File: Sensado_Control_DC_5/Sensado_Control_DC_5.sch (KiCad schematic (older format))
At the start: 30 parts

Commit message: Control DC, y Micro placa 5
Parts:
- removed Q? (x3): NMOS, TO_SOT_Packages_THT:TO-220_Vertical, symbol NMOS
- removed Q? (x3): PMOS, TO_SOT_Packages_THT:TO-220_Vertical, symbol PMOS
- removed R? (x15): R, symbol R
- added C1, C2, C3, C5, C6: 0,1uF, Capacitors_SMD:C_0805_HandSoldering, symbol 0,1uF
- added C4: 1nF, Capacitors_SMD:C_1206_HandSoldering, symbol 1nF
- added C7, C8: 18pF, Capacitors_SMD:C_0805_HandSoldering, symbol 18pF
- added C9: 10uF, Capacitors_SMD:C_0805_HandSoldering, symbol 10uF
- added D1, D2, D3: Led_Small_Reg, LEDs:LED_0805, symbol Led_Small_Reg
- added J1, J2, J3: Jumper, Pin_Headers:Pin_Header_Straight_1x02_Pitch2.54mm, symbol Jumper
- added P10: GPIO, Socket_Strips:Socket_Strip_Straight_1x05_Pitch2.54mm, symbol CONN_01X05
- added P11: CONM_R1, Socket_Strips:Socket_Strip_Straight_1x02_Pitch2.54mm, symbol CONN_01X02
- added P2: I_+, Sockets_MOLEX_KK-System:Socket_MOLEX-KK-RM3-96mm_Lock_2pin_straight, symbol CONN_01X02
- added P3: I_-, Sockets_MOLEX_KK-System:Socket_MOLEX-KK-RM3-96mm_Lock_2pin_straight, symbol CONN_01X02
- added P4: POWER, Sockets_MOLEX_KK-System:Socket_MOLEX-KK-RM3-96mm_Lock_2pin_straight, symbol CONN_01X02
- added P5: RS-232, Socket_Strips:Socket_Strip_Straight_1x03_Pitch2.54mm, symbol CONN_01X03
- added P6: I2C, Socket_Strips:Socket_Strip_Straight_1x02_Pitch2.54mm, symbol CONN_01X02
- added P7: SPI, Socket_Strips:Socket_Strip_Straight_1x04_Pitch2.54mm, symbol CONN_01X04
- added P8: GND_REG, Socket_Strips:Socket_Strip_Straight_1x01_Pitch2.54mm, symbol CONN_01X01
- added P9: RESET, Socket_Strips:Socket_Strip_Straight_1x01_Pitch2.54mm, symbol CONN_01X01
- added Q10, Q14, Q15, Q16, Q7, Q8, Q9: PMOS, TO_SOT_Packages_THT:TO-220_Vertical, symbol PMOS
- added Q11, Q12, Q13, Q2, Q3, Q4, Q5: NMOS, TO_SOT_Packages_THT:TO-220_Vertical, symbol NMOS
- added R10, R11, R13, R14, R15, R16, R18, R19, R2, R20, R21, R23, R24, R25, R26, R27, R28, R29, R3, R30, R31, R32, R33, R34, R35, R36, R37, R38, R39, R4, R40, R41, R5, R8, R9: R, Resistors_THT:R_Axial_DIN0207_L6.3mm_D2.5mm_P7.62mm_Horizontal, symbol R
- added R42, R44, R47: 10K, Resistors_SMD:R_0805_HandSoldering, symbol 10K
- added R43, R45, R46: 1K, Resistors_SMD:R_0805_HandSoldering, symbol 1K
- added U1: Atmega328PA, Housings_QFP:LQFP-32_7x7mm_Pitch0.8mm, symbol Atmega328PA
- added U2: ACS_712, Housings_SOIC:SOIC-8_3.9x4.9mm_Pitch1.27mm, symbol ACS_712
- added U3: LD1117S50TR_FINAL, TO_SOT_Packages_SMD:SOT-223, symbol LD1117S50TR_FINAL
- added Y1: AMB3_16M, symbol AMB3_16M
- P1: renamed from P?; value CONN_01X02 -> R_FUENTE_CON; footprint (none) -> Sockets_MOLEX_KK-System:Socket_MOLEX-KK-RM3-96mm_Lock_2pin_straight
- R1, R12, R17, R22, R7: renamed from R?; footprint (none) -> Resistors_THT:R_Axial_DIN0207_L6.3mm_D2.5mm_P7.62mm_Horizontal
- R6: renamed from R?; footprint (none) -> Resistors_THT:R_Axial_DIN0207_L6.3mm_D2.5mm_P10.16mm_Horizontal
- gave numbers to parts that had none: 2
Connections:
- net labels added: 5V, CLK1, CLK2, I_SENS+, I_SENS-, MISO, MOSI, REG1_1, REG1_2, REG1_3, REG1_4, REG1_5, RESET, RXD, SCK, SCL, SCL_E, SDA, SDA_E, TXD, VCONTROL_2, VCONTROL_3, VCONTROL_4, VCONTROL_5, VCONTROL_6, VCONTROL_7, VCONTROL_8, VOUT_SENS, V_FUENTE, ~SS
- wire segments 62 -> 244
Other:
- note added: "Conector Progrmador \ndel Microcontrolador \n- Debuger (RS-232)"
- note added: "Conectores Fuente Conmutada"
- note added: "GPIO"
- note added: "In Sensor de Corriente"
- note added: "Out Sensor de Corriente"
- note added: "Pines de Alimentacion"
- note added: "Quemador Bootloader -\nComunicacion SPI"
- note added: "Regulador\n"
- note added: "Reset Micro"
- note added: "Resistencias Pull-up\n- Comunicacion I2C"
- note added: "Resistor Variable 1"
- note added: "Resistor Variable 2\n"
- note added: "Resistor Variable 3\n"
- note added: "Resistor Variable 4\n"
- note added: "Resistor Variable 5"
- note added: "Resistor Variable 6"
- note added: "Resistor Variable 7"
- note added: "Resistor Variable 8"
- note added: "Sensor de Corriente\n"
- note added: "Señal de Reloj Externo \n Atmega"
- note added: "Tierra para Alimentacion \nExterna al Regulador"

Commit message: Version avanzada PCB
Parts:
- removed C4: 1nF, Capacitors_SMD:C_1206_HandSoldering, symbol 1nF
- removed P11: CONM_R1, Socket_Strips:Socket_Strip_Straight_1x02_Pitch2.54mm, symbol CONN_01X02
- added C4: 1nF_THT, Capacitors_THT:C_Disc_D5.0mm_W2.5mm_P2.50mm, symbol 1nF_THT
- R6: footprint Resistors_THT:R_Axial_DIN0207_L6.3mm_D2.5mm_P10.16mm_Horizontal -> Resistors_THT:R_Axial_DIN0207_L6.3mm_D2.5mm_P7.62mm_Horizontal
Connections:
- wire segments 244 -> 242
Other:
- note removed: "Conectores Fuente Conmutada"
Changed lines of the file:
@@
 F 0 "R6" V 1210 1030 50  0000 C CNN
 F 1 "R" V 1130 1030 50  0000 C CNN
-F 2 "Resistors_THT:R_Axial_DIN0207_L6.3mm_D2.5mm_P10.16mm_Horizontal" V 1060 1030 50  0001 C CNN
+F 2 "Resistors_THT:R_Axial_DIN0207_L6.3mm_D2.5mm_P7.62mm_Horizontal" V 1060 1030 50  0001 C CNN
 F 3 "" H 1130 1030 50  0000 C CNN
 	1    1130 1030
@@
 VOUT
 Text Label 660  2140 0    39   ~ 0
-VCONTROL_1
+VCONTROL_5
 Text Notes 660  1580 0    39   ~ 0
 Resistor Variable 1
@@
 $EndComp
 $Comp
-L 1nF C4
-U 1 1 59D40CE7
-P 5130 1220
-F 0 "C4" H 5140 1290 50  0000 L CNN
-F 1 "1nF" H 5140 1140 50  0000 L CNN
-F 2 "Capacitors_SMD:C_1206_HandSoldering" H 5040 1190 50  0001 C CNN
-F 3 "" H 5140 1290 50  0000 C CNN
-	1    5130 1220
-	1    0    0    -1
-$EndComp
-$Comp
 L 0,1uF C5
 U 1 1 59D44EBB
@@
 	1    0    0    -1
 $EndComp
+Text Label 4660 4500 0    39   ~ 0
+V_FUENTE
 Text Label 4660 4400 0    39   ~ 0
-V_FUENTE
-Text Label 4660 4500 0    39   ~ 0
 GND
 Text Label 4680 5330 0    39   ~ 0
@@
 VOUT
 Text Label 660  3410 0    39   ~ 0
-VCONTROL_2
+VCONTROL_4
 Text Notes 660  2850 0    39   ~ 0
 Resistor Variable 2\n
@@
 VOUT
 Text Label 680  5900 0    39   ~ 0
-VCONTROL_4
+VCONTROL_6
 Text Notes 680  5380 0    39   ~ 0
 Resistor Variable 4\n
@@
 VOUT
 Text Label 690  7130 0    39   ~ 0
-VCONTROL_5
+VCONTROL_8
 Text Notes 690  6620 0    39   ~ 0
 Resistor Variable 5
@@
 VOUT
 Text Label 2520 4660 0    39   ~ 0
-VCONTROL_6
+VCONTROL_7
 Text Notes 2540 4160 0    39   ~ 0
 Resistor Variable 6
@@
 VOUT
 Text Label 2530 5900 0    39   ~ 0
-VCONTROL_7
+VCONTROL_2
 Text Notes 2530 5380 0    39   ~ 0
 Resistor Variable 7
@@
 VOUT
 Text Label 2540 7130 0    39   ~ 0
-VCONTROL_8
+VCONTROL_1
 Text Notes 2540 6620 0    39   ~ 0
 Resistor Variable 8
@@
 Text Notes 6120 4060 0    39   ~ 0
 Reset Micro
-$Comp
-L CONN_01X02 P11
-U 1 1 59CF6F3A
-P 6100 5160
-F 0 "P11" H 6100 5310 50  0000 C CNN
-F 1 "CONM_R1" V 6200 5160 50  0000 C CNN
-F 2 "Socket_Strips:Socket_Strip_Straight_1x02_Pitch2.54mm" H 6100 5160 50  0001 C CNN
-F 3 "" H 6100 5160 50  0000 C CNN
-	1    6100 5160
-	1    0    0    -1
-$EndComp
-Text Notes 5590 4870 0    39   ~ 0
-Conectores Fuente Conmutada
-Wire Wire Line
-	5900 5110 5710 5110
-Wire Wire Line
-	5900 5210 5710 5210
-Text Label 5710 5110 0    39   ~ 0
-VOUT
-Text Label 5710 5210 0    39   ~ 0
-VFB
 Text Label 4840 7120 0    39   ~ 0
 5V
@@
 	1    0    0    -1
 $EndComp
+$Comp
+L 1nF_THT C4
+U 1 1 59D0DD60
+P 5130 1220
+F 0 "C4" H 5140 1290 50  0000 L CNN
+F 1 "1nF_THT" H 5140 1140 50  0000 L CNN
+F 2 "Capacitors_THT:C_Disc_D5.0mm_W2.5mm_P2.50mm" H 5040 1190 50  0001 C CNN
+F 3 "" H 5140 1290 50  0000 C CNN
+	1    5130 1220
+	1    0    0    -1
+$EndComp
+Text Label 5140 910  0    39   ~ 0
+5V
 $EndSCHEMATC

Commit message: Isletas y clock añadido a la PCB
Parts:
- removed C7, C8: 18pF, Capacitors_SMD:C_0805_HandSoldering, symbol 18pF
- removed Y1: AMB3_16M, symbol AMB3_16M
- added C7, C8: 8pF, Capacitors_SMD:C_0805_HandSoldering, symbol 8pF
- added Y1: XRCHA_16M, Huellas:Crystal_SMD_XRCHA_Murata_Serie_W2,5mm_L2,0mm, symbol XRCHA_16M
- U1: footprint Housings_QFP:LQFP-32_7x7mm_Pitch0.8mm -> Housings_QFP:TQFP-32_7x7mm_Pitch0.8mm
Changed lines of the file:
@@
 F 0 "U1" H 3820 1500 60  0000 C CNN
 F 1 "Atmega328PA" H 3750 2490 60  0000 C CNN
-F 2 "Housings_QFP:LQFP-32_7x7mm_Pitch0.8mm" H 3820 2090 60  0001 C CNN
+F 2 "Housings_QFP:TQFP-32_7x7mm_Pitch0.8mm" H 3820 2090 60  0001 C CNN
 F 3 "" H 3820 2090 60  0000 C CNN
 	1    3790 2090
@@
 Text Notes 5680 700  0    39   ~ 0
 Tierra para Alimentacion \nExterna al Regulador
-$Comp
-L 18pF C7
-U 1 1 59CEE49D
-P 5740 3590
-F 0 "C7" H 5750 3660 50  0000 L CNN
-F 1 "18pF" H 5750 3510 50  0000 L CNN
-F 2 "Capacitors_SMD:C_0805_HandSoldering" H 5650 3560 50  0001 C CNN
-F 3 "" H 5750 3660 50  0000 C CNN
-F 4 "399-1113-2-ND" H 5850 3760 39  0001 C CNN "CAP CER 22PF 50V C0G/NP0 0805"
-	1    5740 3590
-	1    0    0    -1
-$EndComp
-$Comp
-L 18pF C8
-U 1 1 59CF0165
-P 6510 3620
-F 0 "C8" H 6520 3690 50  0000 L CNN
-F 1 "18pF" H 6520 3540 50  0000 L CNN
-F 2 "Capacitors_SMD:C_0805_HandSoldering" H 6420 3590 50  0001 C CNN
-F 3 "" H 6520 3690 50  0000 C CNN
-F 4 "399-1113-2-ND" H 6620 3790 39  0001 C CNN "CAP CER 22PF 50V C0G/NP0 0805"
-	1    6510 3620
-	1    0    0    -1
-$EndComp
-$Comp
-L AMB3_16M Y1
-U 1 1 59CF0C6D
-P 6100 3340
-F 0 "Y1" H 6100 3440 50  0000 C CNN
-F 1 "AMB3_16M" H 6100 3240 50  0000 C CNN
-F 2 "" H 6100 3340 50  0000 C CNN
-F 3 "" H 6100 3340 50  0000 C CNN
-	1    6100 3340
-	1    0    0    -1
-$EndComp
 Text Label 5900 3860 0    39   ~ 0
 GND
@@
 Text Label 5140 910  0    39   ~ 0
 5V
+$Comp
+L XRCHA_16M Y1
+U 1 1 59D118B1
+P 6100 3340
+F 0 "Y1" H 6100 3440 50  0000 C CNN
+F 1 "XRCHA_16M" H 6100 3240 50  0000 C CNN
+F 2 "Huellas:Crystal_SMD_XRCHA_Murata_Serie_W2,5mm_L2,0mm" H 6000 3340 50  0001 C CNN
+F 3 "" H 6100 3340 50  0000 C CNN
+	1    6100 3340
+	1    0    0    -1
+$EndComp
+$Comp
+L 8pF C8
+U 1 1 59D13289
+P 6510 3620
+F 0 "C8" H 6520 3690 50  0000 L CNN
+F 1 "8pF" H 6520 3540 50  0000 L CNN
+F 2 "Capacitors_SMD:C_0805_HandSoldering" H 6420 3590 50  0001 C CNN
+F 3 "" H 6520 3690 50  0000 C CNN
+F 4 "399-1113-2-ND" H 6620 3790 39  0001 C CNN "CAP CER 22PF 50V C0G/NP0 0805"
+	1    6510 3620
+	1    0    0    -1
+$EndComp
+$Comp
+L 8pF C7
+U 1 1 59D14715
+P 5740 3590
+F 0 "C7" H 5750 3660 50  0000 L CNN
+F 1 "8pF" H 5750 3510 50  0000 L CNN
+F 2 "Capacitors_SMD:C_0805_HandSoldering" H 5650 3560 50  0001 C CNN
+F 3 "" H 5750 3660 50  0000 C CNN
+F 4 "399-1113-2-ND" H 5850 3760 39  0001 C CNN "CAP CER 22PF 50V C0G/NP0 0805"
+	1    5740 3590
+	1    0    0    -1
+$EndComp
 $EndSCHEMATC

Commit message: PCB mejorada
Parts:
- removed P10: GPIO, Socket_Strips:Socket_Strip_Straight_1x05_Pitch2.54mm, symbol CONN_01X05
- added P10: GPIO, Socket_Strips:Socket_Strip_Straight_1x03_Pitch2.54mm, symbol CONN_01X03
- added R48, R49, R50, R51, R52, R53, R54, R55: 10K, Resistors_SMD:R_0805_HandSoldering, symbol 10K
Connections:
- net REG1_4 is gone; now on net VCONTROL_6: U1.12 (PB0)
- net REG1_5 is gone; now on net VCONTROL_5: U1.13 (PB1)
- net GND: now also R48.2, R49.2, R50.2, R51.2, R52.2, R53.2, R54.2, R55.2
- net REG1_1: now also P10.1 (P1)
- net REG1_2: now also P10.2 (P2)
- net REG1_3: now also P10.3 (P3)
- net VCONTROL_5: no longer U1.22 (ADC7)
- net VCONTROL_6: no longer U1.19 (ADC6)
- net at Q1.1 (G), R1.2: now also R48.1
- net at Q2.1 (G), R2.2: now also R49.1
- net at Q3.1 (G), R3.2: now also R50.1
- net at Q4.1 (G), R4.2: now also R51.1
- net at Q5.1 (G), R5.2: now also R52.1
- net at Q11.1 (G), R27.2: now also R53.1
- net at Q12.1 (G), R28.2: now also R54.1
- net at Q13.1 (G), R29.2: now also R55.1
- no-connect marks 0 -> 2

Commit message: Puertos I2C mejorados
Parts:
- removed P6: I2C, Socket_Strips:Socket_Strip_Straight_1x02_Pitch2.54mm, symbol CONN_01X02
- added P6: I2C, Socket_Strips:Socket_Strip_Straight_2x03_Pitch2.54mm, symbol CONN_02X03
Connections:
- net SCL: now also P6.1 (P1), P6.3 (P3), P6.5 (P5)
- net SDA: now also P6.2 (P2), P6.4 (P4), P6.6 (P6)
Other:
- moved on the sheet: J1, J2
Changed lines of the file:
@@
 Text Label 4630 6250 0    39   ~ 0
 SCK
-$Comp
-L CONN_01X02 P6
-U 1 1 59DABC73
-P 5200 6890
-F 0 "P6" H 5200 7040 50  0000 C CNN
-F 1 "I2C" V 5300 6890 50  0000 C CNN
-F 2 "Socket_Strips:Socket_Strip_Straight_1x02_Pitch2.54mm" H 5200 6890 50  0001 C CNN
-F 3 "" H 5200 6890 50  0000 C CNN
-	1    5200 6890
-	1    0    0    -1
-$EndComp
-Text Label 4660 6840 0    39   ~ 0
+Text Label 6400 6760 2    39   ~ 0
 SDA
-Text Label 4660 6940 0    39   ~ 0
+Text Label 5220 6760 0    39   ~ 0
 SCL
 Text Notes 4560 6610 0    39   ~ 0
@@
 L Jumper J1
 U 1 1 59DB5A77
-P 5830 6830
-F 0 "J1" V 5640 6760 50  0000 L CNN
-F 1 "Jumper" V 5720 6750 50  0000 L CNN
-F 2 "Pin_Headers:Pin_Header_Straight_1x02_Pitch2.54mm" H 5830 6830 50  0001 C CNN
-F 3 "" H 5830 6830 50  0000 C CNN
-	1    5830 6830
+P 5900 7370
+F 0 "J1" V 5710 7300 50  0000 L CNN
+F 1 "Jumper" V 5790 7290 50  0000 L CNN
+F 2 "Pin_Headers:Pin_Header_Straight_1x02_Pitch2.54mm" H 5900 7370 50  0001 C CNN
+F 3 "" H 5900 7370 50  0000 C CNN
+	1    5900 7370
 	0    1    1    0
 $EndComp
@@
 L Jumper J2
 U 1 1 59DB5B56
-P 5840 6940
-F 0 "J2" V 5900 6870 50  0000 L CNN
-F 1 "Jumper" V 5970 6870 50  0000 L CNN
-F 2 "Pin_Headers:Pin_Header_Straight_1x02_Pitch2.54mm" H 5840 6940 50  0001 C CNN
-F 3 "" H 5840 6940 50  0000 C CNN
-	1    5840 6940
+P 5910 7480
+F 0 "J2" V 5970 7410 50  0000 L CNN
+F 1 "Jumper" V 6040 7410 50  0000 L CNN
+F 2 "Pin_Headers:Pin_Header_Straight_1x02_Pitch2.54mm" H 5910 7480 50  0001 C CNN
+F 3 "" H 5910 7480 50  0000 C CNN
+	1    5910 7480
 	0    1    1    0
 $EndComp
-Text Label 5430 6830 0    39   ~ 0
+Text Label 5500 7370 0    39   ~ 0
 SDA_E
-Text Label 5430 6940 0    39   ~ 0
+Text Label 5500 7480 0    39   ~ 0
 SCL_E
-Text Label 6120 6830 0    39   ~ 0
+Text Label 6190 7370 0    39   ~ 0
 SDA
-Text Label 6120 6940 0    39   ~ 0
+Text Label 6190 7480 0    39   ~ 0
 SCL
 Text Label 4350 660  0    39   ~ 0
@@
 	2490 3940 2490 1500
 Wire Wire Line
-	3220 2200 2610 2200
-Wire Wire Line
-	3220 2400 2610 2400
-Wire Wire Line
-	4950 2000 4340 2000
+	2610 2200 3220 2200
+Wire Wire Line
+	2610 2400 3220 2400
+Wire Wire Line
+	4340 2000 4950 2000
 Wire Wire Line
 	2880 1900 3220 1900
@@
 	5020 6250 4630 6250
 Wire Notes Line
-	4330 6470 6300 6470
-Wire Wire Line
-	5000 6840 4660 6840
-Wire Wire Line
-	5000 6940 4660 6940
+	4330 6470 6490 6470
+Wire Wire Line
+	6060 6760 6400 6760
+Wire Wire Line
+	5560 6760 5220 6760
 Wire Notes Line
 	4330 6470 4330 7690
@@
 Connection ~ 4950 7610
 Wire Wire Line
-	5430 6830 5730 6830
-Wire Wire Line
-	5430 6940 5740 6940
-Wire Wire Line
-	5930 6830 6120 6830
-Wire Wire Line
-	5940 6940 6120 6940
-Wire Notes Line
-	6300 6470 6300 7690
-Wire Notes Line
-	6300 7690 4330 7690
+	5500 7370 5800 7370
+Wire Wire Line
+	5500 7480 5810 7480
+Wire Wire Line
+	6000 7370 6190 7370
+Wire Wire Line
+	6010 7480 6190 7480
+Wire Notes Line
+	4330 7690 6490 7690
 Wire Wire Line
 	5040 660  5040 910
@@
 Wire Wire Line
 	2860 7580 2960 7580
+$Comp
+L CONN_02X03 P6
+U 1 1 59D41214
+P 5810 6760
+F 0 "P6" H 5810 6960 50  0000 C CNN
+F 1 "I2C" H 5810 6560 50  0000 C CNN
+F 2 "Socket_Strips:Socket_Strip_Straight_2x03_Pitch2.54mm" H 5810 5560 50  0001 C CNN
+F 3 "" H 5810 5560 50  0000 C CNN
+	1    5810 6760
+	1    0    0    -1
+$EndComp
+Text Label 5220 6660 0    39   ~ 0
+SCL
+Wire Wire Line
+	5560 6660 5220 6660
+Text Label 5220 6860 0    39   ~ 0
+SCL
+Wire Wire Line
+	5560 6860 5220 6860
+Text Label 6400 6660 2    39   ~ 0
+SDA
+Wire Wire Line
+	6060 6660 6400 6660
+Text Label 6400 6860 2    39   ~ 0
+SDA
+Wire Wire Line
+	6060 6860 6400 6860
+Wire Notes Line
+	6490 7690 6490 6470
 $EndSCHEMATC

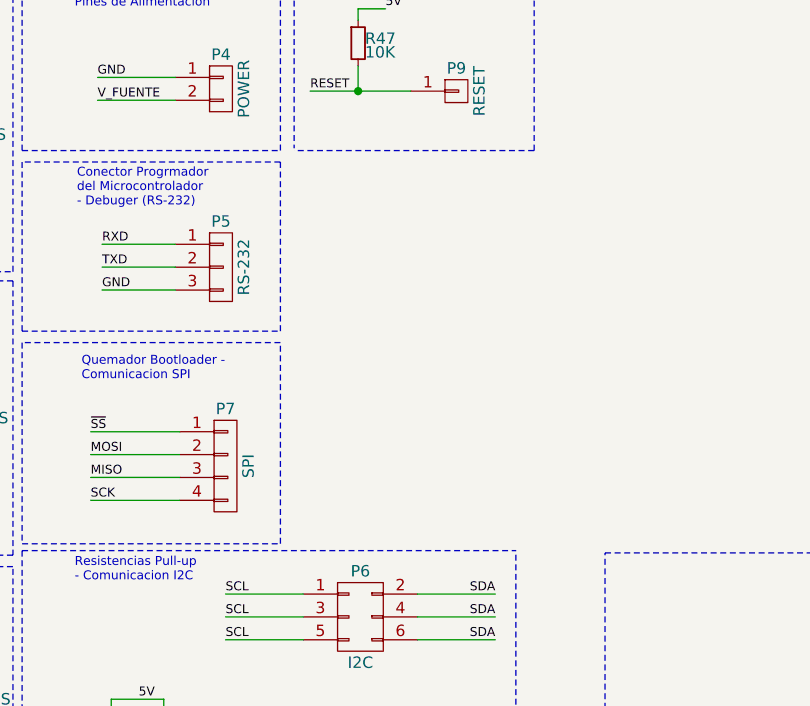
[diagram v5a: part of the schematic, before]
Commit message: Version PCB con tornillos incluidos
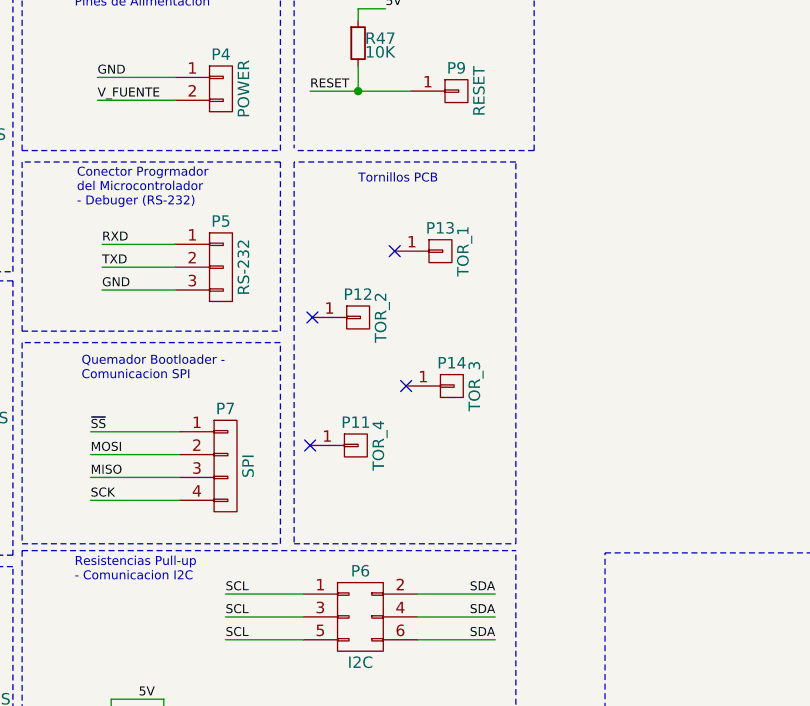
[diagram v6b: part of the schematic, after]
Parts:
- added P11: TOR_4, Mounting_Holes:MountingHole_3.2mm_M3_Pad_Via, symbol CONN_01X01
- added P12: TOR_2, Mounting_Holes:MountingHole_3.2mm_M3_Pad_Via, symbol CONN_01X01
- added P13: TOR_1, Mounting_Holes:MountingHole_3.2mm_M3_Pad_Via, symbol CONN_01X01
- added P14: TOR_3, Mounting_Holes:MountingHole_3.2mm_M3_Pad_Via, symbol CONN_01X01
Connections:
- no-connect marks 2 -> 6
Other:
- note added: "Tornillos PCB"
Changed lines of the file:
@@
 Wire Notes Line
 	6490 7690 6490 6470
+$Comp
+L CONN_01X01 P12
+U 1 1 59D5E232
+P 5800 5450
+F 0 "P12" H 5800 5550 50  0000 C CNN
+F 1 "TOR_2" V 5900 5450 50  0000 C CNN
+F 2 "Mounting_Holes:MountingHole_3.2mm_M3_Pad_Via" H 5800 5450 50  0001 C CNN
+F 3 "" H 5800 5450 50  0000 C CNN
+	1    5800 5450
+	1    0    0    -1
+$EndComp
+$Comp
+L CONN_01X01 P13
+U 1 1 59D5EBFE
+P 6160 5160
+F 0 "P13" H 6160 5260 50  0000 C CNN
+F 1 "TOR_1" V 6260 5160 50  0000 C CNN
+F 2 "Mounting_Holes:MountingHole_3.2mm_M3_Pad_Via" H 6160 5160 50  0001 C CNN
+F 3 "" H 6160 5160 50  0000 C CNN
+	1    6160 5160
+	1    0    0    -1
+$EndComp
+$Comp
+L CONN_01X01 P14
+U 1 1 59D5ED56
+P 6210 5750
+F 0 "P14" H 6210 5850 50  0000 C CNN
+F 1 "TOR_3" V 6310 5750 50  0000 C CNN
+F 2 "Mounting_Holes:MountingHole_3.2mm_M3_Pad_Via" H 6210 5750 50  0001 C CNN
+F 3 "" H 6210 5750 50  0000 C CNN
+	1    6210 5750
+	1    0    0    -1
+$EndComp
+$Comp
+L CONN_01X01 P11
+U 1 1 59D5ED5C
+P 5790 6010
+F 0 "P11" H 5790 6110 50  0000 C CNN
+F 1 "TOR_4" V 5890 6010 50  0000 C CNN
+F 2 "Mounting_Holes:MountingHole_3.2mm_M3_Pad_Via" H 5790 6010 50  0001 C CNN
+F 3 "" H 5790 6010 50  0000 C CNN
+	1    5790 6010
+	1    0    0    -1
+$EndComp
+Wire Notes Line
+	5520 4770 5520 6440
+Wire Notes Line
+	5520 6440 6490 6440
+Wire Notes Line
+	6490 6440 6490 4770
+Wire Notes Line
+	6490 4770 5520 4770
+Text Notes 5800 4870 0    39   ~ 0
+Tornillos PCB
+NoConn ~ 5590 6010
+NoConn ~ 6010 5750
+NoConn ~ 5600 5450
+NoConn ~ 5960 5160
 $EndSCHEMATC

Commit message: Version para placa
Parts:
- added W1, W2, W3, W4: TEST_1P, Measurement_Points:Measurement_Point_Round-TH_Small, symbol TEST_1P
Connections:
- net 5V: now also W2.1
- net VFB: now also W4.1
- net VOUT: now also W3.1
- net V_FUENTE: now also W1.1
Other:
- note added: "Test Points"
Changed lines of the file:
@@
 In Sensor de Corriente
-$Comp
-L ACS_712 U2
-U 1 1 59D369E2
-P 4500 1040
-F 0 "U2" H 4500 1260 39  0000 C CNN
-F 1 "ACS_712" H 4500 800 39  0000 C CNN
-F 2 "Housings_SOIC:SOIC-8_3.9x4.9mm_Pitch1.27mm" H 4500 1270 39  0001 C CNN
-F 3 "" H 4500 1270 39  0000 C CNN
-	1    4500 1040
-	1    0    0    -1
-$EndComp
 $Comp
 L 0,1uF C5
@@
 NoConn ~ 5600 5450
 NoConn ~ 5960 5160
+$Comp
+L ACS_712 U2
+U 1 1 59D461A2
+P 4500 1040
+F 0 "U2" H 4500 1270 39  0000 C CNN
+F 1 "ACS_712" H 4500 800 39  0000 C CNN
+F 2 "Housings_SOIC:SOIC-8_3.9x4.9mm_Pitch1.27mm" H 4500 1270 39  0001 C CNN
+F 3 "" H 4500 1270 39  0000 C CNN
+	1    4500 1040
+	1    0    0    -1
+$EndComp
+Wire Notes Line
+	7340 1430 7340 570
+Wire Notes Line
+	7340 570  8860 570
+Wire Notes Line
+	7340 1430 8860 1430
+$Comp
+L TEST_1P W1
+U 1 1 59D92BFD
+P 7640 970
+F 0 "W1" H 7640 1240 50  0000 C CNN
+F 1 "TEST_1P" H 7640 1170 50  0000 C CNN
+F 2 "Measurement_Points:Measurement_Point_Round-TH_Small" H 7840 970 50  0001 C CNN
+F 3 "" H 7840 970 50  0000 C CNN
+	1    7640 970
+	1    0    0    -1
+$EndComp
+$Comp
+L TEST_1P W2
+U 1 1 59D92DB8
+P 7970 970
+F 0 "W2" H 7970 1240 50  0000 C CNN
+F 1 "TEST_1P" H 7970 1170 50  0000 C CNN
+F 2 "Measurement_Points:Measurement_Point_Round-TH_Small" H 8170 970 50  0001 C CNN
+F 3 "" H 8170 970 50  0000 C CNN
+	1    7970 970
+	1    0    0    -1
+$EndComp
+$Comp
+L TEST_1P W3
+U 1 1 59D92EE0
+P 8300 970
+F 0 "W3" H 8300 1240 50  0000 C CNN
+F 1 "TEST_1P" H 8300 1170 50  0000 C CNN
+F 2 "Measurement_Points:Measurement_Point_Round-TH_Small" H 8500 970 50  0001 C CNN
+F 3 "" H 8500 970 50  0000 C CNN
+	1    8300 970
+	1    0    0    -1
+$EndComp
+$Comp
+L TEST_1P W4
+U 1 1 59D92EE6
+P 8630 970
+F 0 "W4" H 8630 1240 50  0000 C CNN
+F 1 "TEST_1P" H 8630 1170 50  0000 C CNN
+F 2 "Measurement_Points:Measurement_Point_Round-TH_Small" H 8830 970 50  0001 C CNN
+F 3 "" H 8830 970 50  0000 C CNN
+	1    8630 970
+	1    0    0    -1
+$EndComp
+Wire Wire Line
+	7640 970  7640 1230
+Wire Wire Line
+	7970 970  7970 1230
+Wire Wire Line
+	8300 970  8300 1230
+Wire Wire Line
+	8630 970  8630 1230
+Wire Notes Line
+	8860 1430 8860 570
+Text Label 7640 1230 1    39   ~ 0
+V_FUENTE
+Text Label 7970 1230 1    39   ~ 0
+5V
+Text Label 8300 1230 1    39   ~ 0
+VOUT
+Text Label 8630 1230 1    39   ~ 0
+VFB
+Text Notes 7690 1350 0    39   ~ 0
+Test Points
 $EndSCHEMATC
